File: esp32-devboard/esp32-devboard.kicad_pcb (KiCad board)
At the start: 2 copper layers, 79.4 x 40.6 mm, 26 parts, among them J1 Conn_01x40, J2 Conn_01x40, J3 USB_B_Micro, J4 RJ12, J5 Barrel_Jack_Switch, J6 Conn_01x04, J7 Conn_01x04, J8 Conn_01x03, J9 Conn_01x02, SW1 SW_Push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

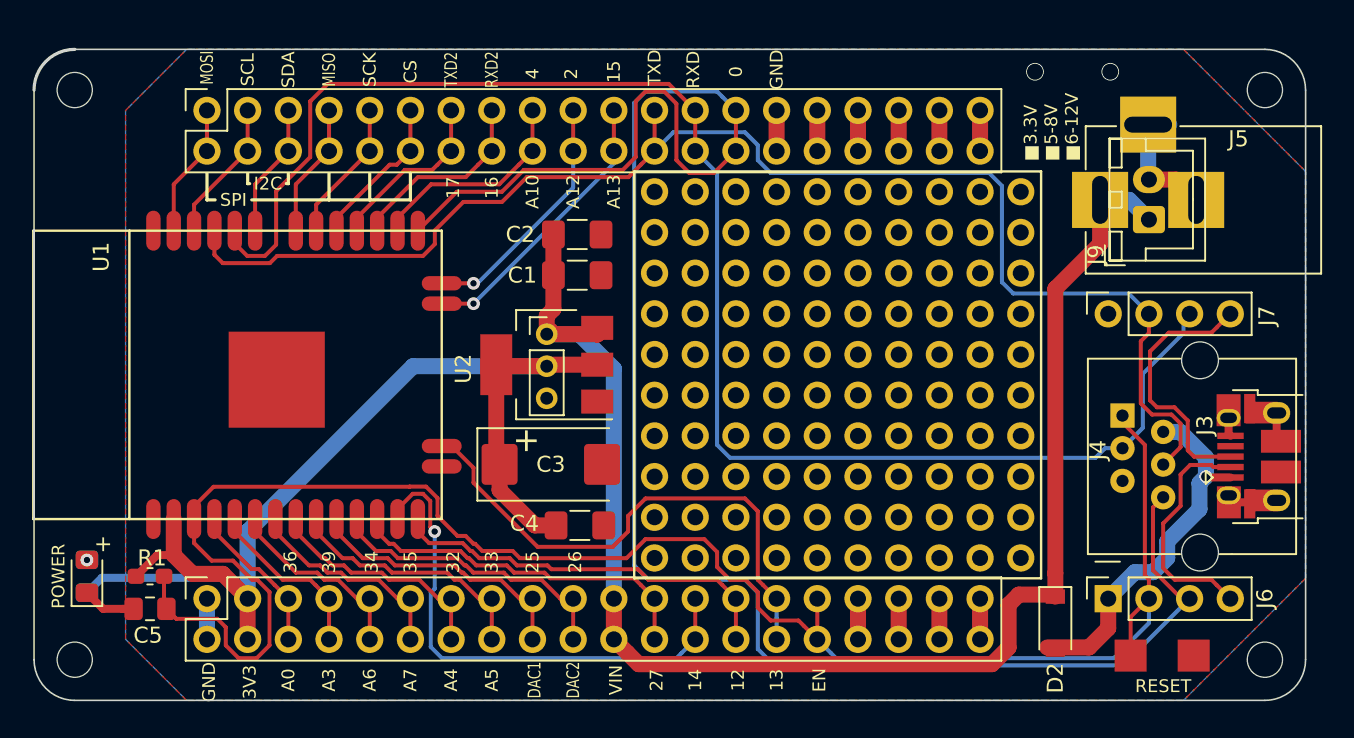
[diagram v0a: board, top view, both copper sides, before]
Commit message: usbesp-rj12 moved from other project
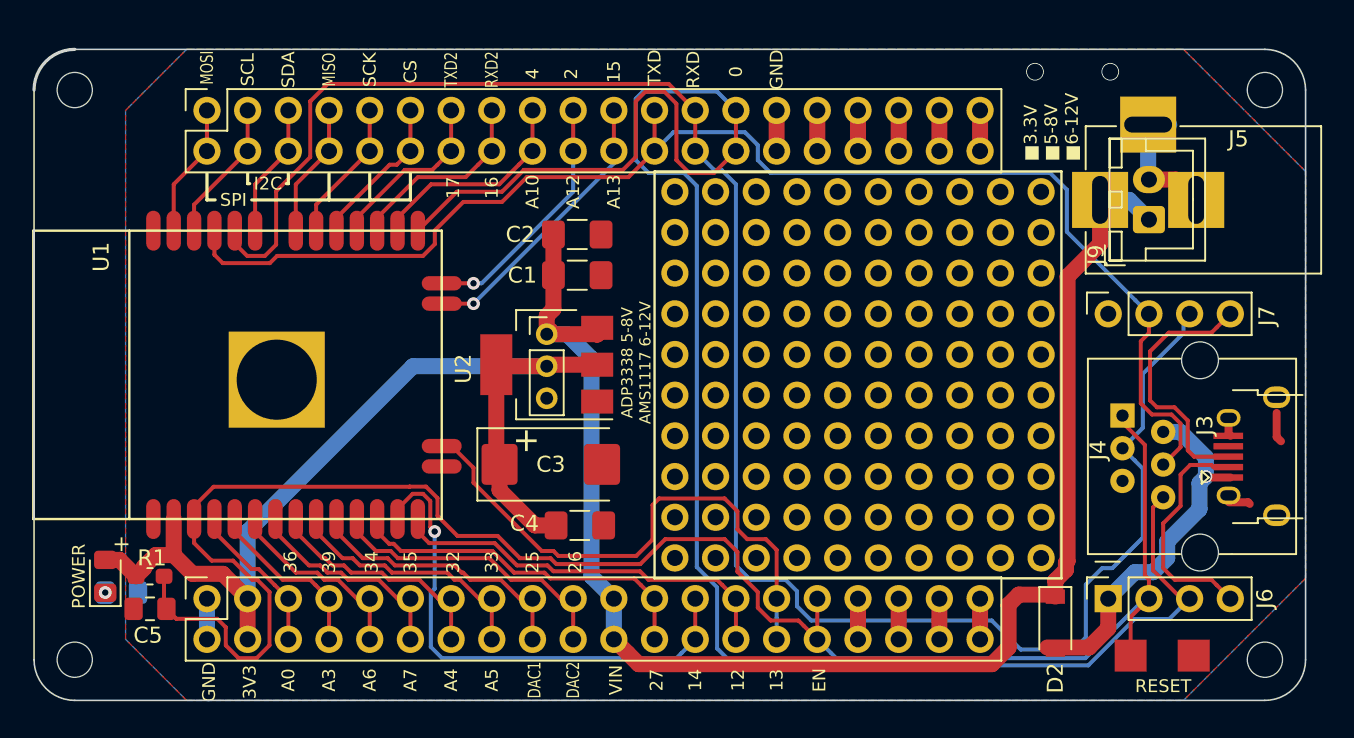
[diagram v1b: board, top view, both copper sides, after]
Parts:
- J3: footprint Connector_USB:USB_Micro-B_Amphenol_10103594-0001LF_Horizontal -> lib:USB_Micro-B_Horizontal
- moved R3 2.39 mm to (121.7, 106.3), turned to 0 degrees
- moved JX 1.27 mm to (179.1, 81.3)
- moved D1 1.14 mm to (120.7, 105.3)
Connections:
- D1 pad 1: GND -> Net-(D1-Pad1)
- D1 pad 2: Net-(D1-Pad2) -> /3V3
- R3 pad 1: /3V3 -> Net-(D1-Pad1)
- R3 pad 2: Net-(D1-Pad2) -> GND
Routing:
- net /RXD: track 96.3 -> 117.8 mm
- net /3V3: track 70.5 -> 62.0 mm
- net GND: track 21.0 -> 17.7 mm
- net /TXD: track 87.1 -> 85.1 mm
- net /IO13: track 33.5 -> 34.6 mm
- net /IO0: track 117.3 -> 116.5 mm
- net Net-(D1-Pad2): vias 1 -> 0
- net Net-(D1-Pad1): vias 0 -> 1
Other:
- board text added: "ADP3338 5-8V AMS1117 6-12V"

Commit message: PCB update
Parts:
- removed D2: D_Schottky, Diode_SMD:D_SOD-123
- added C6: C, Capacitor_SMD:C_0805_2012Metric_Pad1.15x1.40mm_HandSolder, B.Cu at (189.2, 109.5)
- added C7: C, Capacitor_SMD:C_1206_3216Metric_Pad1.42x1.75mm_HandSolder, B.Cu at (186.6, 110.0)
- added J10: Conn_01x02, Connector_PinSocket_2.54mm:PinSocket_1x02_P2.54mm_Vertical, F.Cu at (191.8, 101.6)
- added J11: Conn_01x02, Connector_PinSocket_2.54mm:PinSocket_1x02_P2.54mm_Vertical, F.Cu at (191.8, 88.9)
- added J12: TPS2065DBVR, Package_TO_SOT_SMD:SOT-23-5_HandSoldering, B.Cu at (187.9, 105.6)
- added J13: Conn_01x01, Connector_PinHeader_2.00mm:PinHeader_1x01_P2.00mm_Vertical, F.Cu at (186.7, 91.7)
- added J14: Conn_01x01, Connector_PinHeader_2.00mm:PinHeader_1x01_P2.00mm_Vertical, F.Cu at (184.2, 98.8)
- added SW2: SW_SPDT, Connector_PinSocket_2.54mm:PinSocket_1x03_P2.54mm_Vertical, F.Cu at (184.2, 105.4)
- J6, J7: value Conn_01x04 -> Conn_01x02; footprint Connector_PinSocket_2.54mm:PinSocket_1x04_P2.54mm_Vertical -> Connector_PinSocket_2.54mm:PinSocket_1x02_P2.54mm_Vertical
- R3: moved to F.Cu
- moved J6 5.16 mm to (184.2, 101.6)
- moved R3 4.55 mm to (123.4, 110.5)
- moved SW1 2.84 mm to (189.4, 109.7), turned to 270 degrees
- moved J3 2.67 mm to (192.7, 95.1)
- moved J4 2.54 mm to (184.2, 92.7)
- moved J7 0.89 mm to (184.2, 88.9)
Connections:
- J5 pad 1: /VIN -> /VEXT
- J9 pad 1: /VIN -> /VEXT
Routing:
- net GND: track 17.7 -> 118.7 mm, vias 2 -> 7
- net /VEXT: track 0.00 -> 30.7 mm
- net /VIN: track 94.3 -> 66.4 mm
- net /EN: track 110.4 -> 123.7 mm
- net /IO0: track 116.5 -> 125.8 mm
- net /VBUS: track 23.3 -> 31.4 mm, vias 1 -> 0
- net /D-: track 14.7 -> 22.7 mm, vias 0 -> 1
- net /TXD: track 85.1 -> 92.6 mm
- net /USB_PWR: track 0.00 -> 5.12 mm
- net Net-(D1-Pad1): track 0.00 -> 4.91 mm, vias 1 -> 0
- net /RXD: track 117.8 -> 115.4 mm
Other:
- board text added: "AP7361-33E:5V ADP3338:5-8V AMS1117:6-12V"
- board text added: "EXT"
- board text added: "PWR_SRC"
- board text added: "USB"
- board text added: "■3.3V ■5V ■5-8V ■6-12V"
- board text removed: "ADP3338 5-8V AMS1117 6-12V"
- board text removed: "■3.3V ■5-8V ■6-12V"

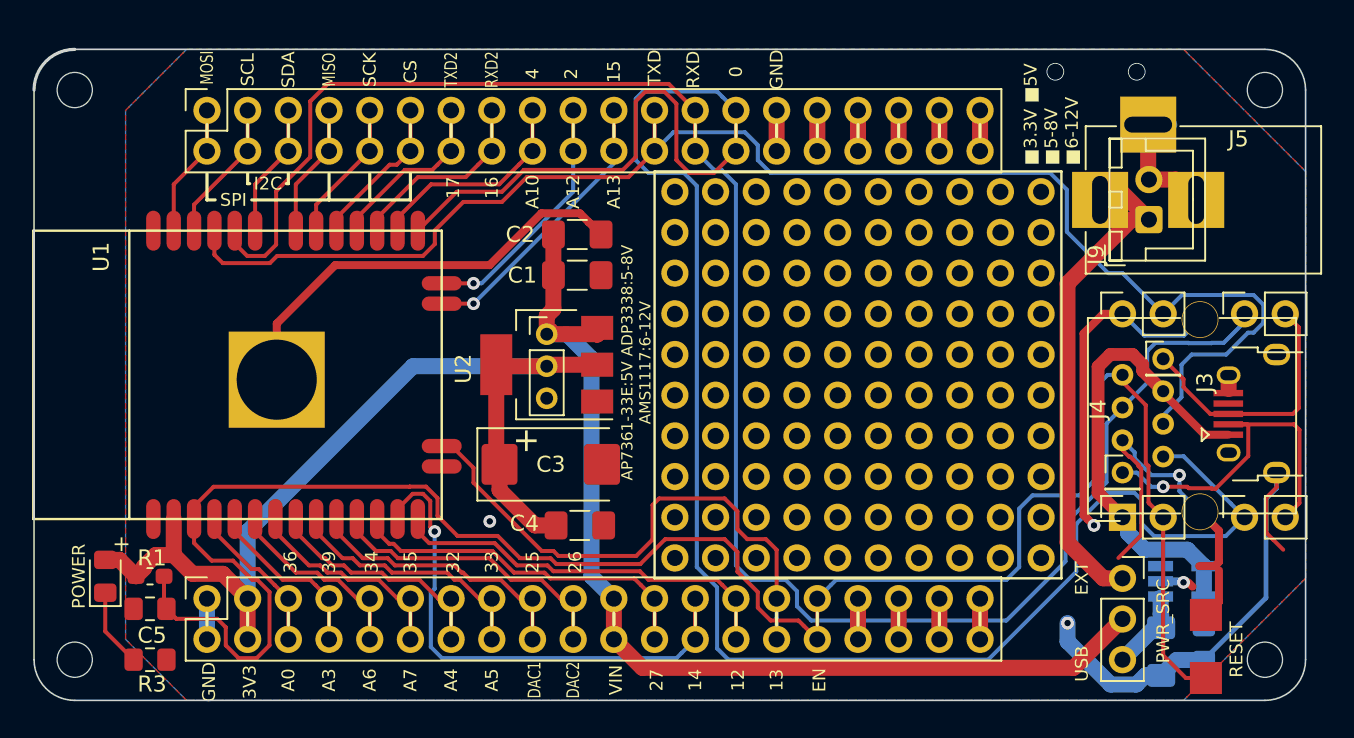
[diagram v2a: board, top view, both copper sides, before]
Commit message: change pinouts
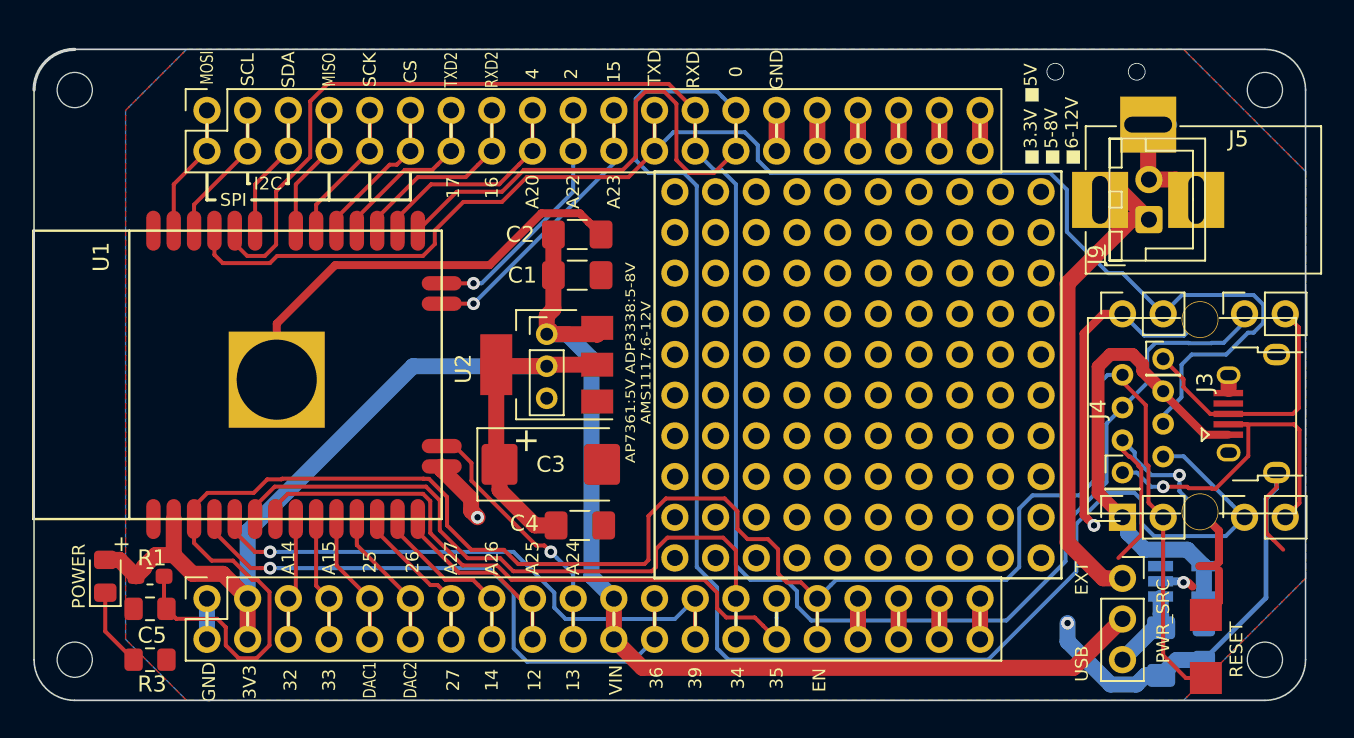
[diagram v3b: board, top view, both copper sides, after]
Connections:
- J1 pad 10: /34 -> /DAC1
- J1 pad 11: /35 -> /DAC2
- J1 pad 12: /35 -> /DAC2
- J1 pad 13: /32 -> /IO27
- J1 pad 14: /32 -> /IO27
- J1 pad 15: /33 -> /IO14
- J1 pad 16: /33 -> /IO14
- J1 pad 17: /DAC1 -> /IO12
- J1 pad 18: /DAC1 -> /IO12
- J1 pad 19: /DAC2 -> /IO13
- J1 pad 20: /DAC2 -> /IO13
- J1 pad 23: /IO27 -> /A0
- J1 pad 24: /IO27 -> /A0
- J1 pad 25: /IO14 -> /A3
- J1 pad 26: /IO14 -> /A3
- J1 pad 27: /IO12 -> /34
- J1 pad 28: /IO12 -> /34
- J1 pad 29: /IO13 -> /35
- J1 pad 30: /IO13 -> /35
- J1 pad 5: /A0 -> /32
- J1 pad 6: /A0 -> /32
- J1 pad 7: /A3 -> /33
- J1 pad 8: /A3 -> /33
- J1 pad 9: /34 -> /DAC1
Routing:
- net /34: track 12.2 -> 42.0 mm
- net /A0: track 9.68 -> 36.8 mm, vias 0 -> 1
- net /35: track 13.5 -> 40.5 mm
- net /A3: track 11.0 -> 35.4 mm, vias 0 -> 1
- net /IO14: track 32.4 -> 11.0 mm, vias 1 -> 0
- net /IO13: track 34.6 -> 16.2 mm, vias 0 -> 1
- net /IO12: track 24.9 -> 12.2 mm
- net /IO27: track 22.4 -> 9.68 mm
- net /DAC2: track 18.6 -> 8.90 mm
- net /DAC1: track 17.3 -> 8.37 mm
- net /33: track 16.0 -> 7.84 mm
- net /32: track 14.8 -> 7.70 mm
- net GND: track 118.7 -> 122.8 mm
- net /EN: track 123.7 -> 127.4 mm
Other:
- board text added: "1"
- board text added: "3"
- board text added: "A14"
- board text added: "A15"
- board text added: "A16"
- board text added: "A17"
- board text added: "A20"
- board text added: "A21"
- board text added: "A22"
- board text added: "A23"
- board text added: "A24"
- board text added: "A25"
- board text added: "A26"
- board text added: "A27"
- board text added: "A28"
- board text added: "A29"
- board text added: "AP7361:5V ADP3338:5-8V AMS1117:6-12V"
- board text removed: "A0"
- board text removed: "A12"
- board text removed: "A3"
- board text removed: "A4"
- board text removed: "A5"
- board text removed: "A6"
- board text removed: "A7"
- board text removed: "AP7361-33E:5V ADP3338:5-8V AMS1117:6-12V"

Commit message: add 3v3 pin for external device
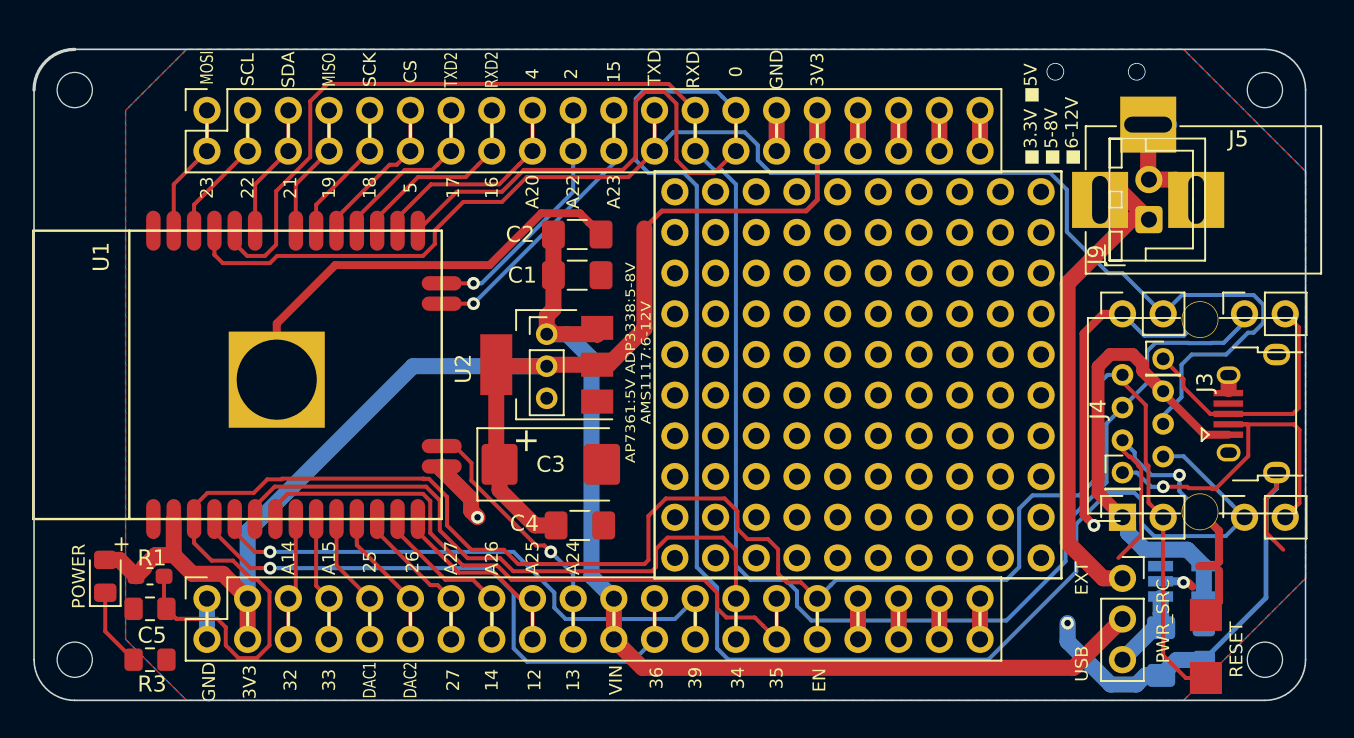
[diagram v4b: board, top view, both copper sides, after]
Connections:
- J2 pad 31: Net-(J2-Pad31) -> /3V3
- J2 pad 32: Net-(J2-Pad31) -> /3V3
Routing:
- net /3V3: track 62.0 -> 89.2 mm
- net Net-(J2-Pad31): track 2.54 -> 0.00 mm
